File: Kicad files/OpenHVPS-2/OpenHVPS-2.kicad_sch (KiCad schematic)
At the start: 67 parts, among them J1 Conn_01x03_Male, J2 Conn_01x03_Male, Q1 FQT7N10, Q2 BC846, Q3 MMDT3906, U1 74HC14, U2 MAX4162, U3 CD14538BM, U4 MAX6008AEUR+T

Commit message: layout chnages
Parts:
- removed J2: Conn_01x03_Male, Connector_PinHeader_2.54mm:PinHeader_1x03_P2.54mm_Vertical, symbol Connector:Conn_01x03_Male
- added J1: Conn_01x03_Male, Connector_PinHeader_2.54mm:PinHeader_1x03_P2.54mm_Vertical, symbol Connector:Conn_01x03_Male
- added JP1: SolderJumper_2_Open, Jumper:SolderJumper-2_P1.3mm_Open_RoundedPad1.0x1.5mm, symbol Jumper:SolderJumper_2_Open
- added R2: 10M, Resistor_SMD:R_1206_3216Metric, symbol Device:R
- R1: renamed from R7; value 4M7 -> 10M
- renumbered C14 to C1, C19 to C10, C5 to C11, C6 to C12, C7 to C13, C8 to C14, C20 to C15, C9 to C16, C10 to C17, C11 to C18, C21 to C19, C15 to C2, C12 to C20, C13 to C21, C16 to C3, C17 to C4, C18 to C5, C1 to C6, C2 to C7, C3 to C8, C4 to C9, D8 to D1, D9 to D2, D1 to D3, D2 to D4, D3 to D5, D4 to D6, D5 to D7, D6 to D8, D7 to D9, FB2 to FB1, FB1 to FB2, H2 to H1, H5 to H2, J1 to J2, R1 to R10, R12 to R11, R13 to R12, R14 to R13, R15 to R14, R16 to R15, R17 to R16, R18 to R17, R19 to R18, R20 to R19, R6 to R20, R5 to R23, R8 to R3, R9 to R4, R10 to R5, R11 to R6, R4 to R7, R3 to R8, R2 to R9, U4 to U1, U1 to U2, U2 to U3, U3 to U4
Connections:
- net +3V3: now also J1.1 (Pin_1)
- net GND: now also J1.2 (Pin_2)
- net at C21.2, D9.3 (K), R1.1: now also R2.1
- net at D2.2 (A), J2.3 (Pin_3), U4.6 (Q): now also J1.3 (Pin_3)
- net at H2.1, R1.2: now also JP1.2 (B)
- new net: JP1.1 (A), R2.2
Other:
- title: OpenRover -> SafePulse
- moved on the sheet: R21

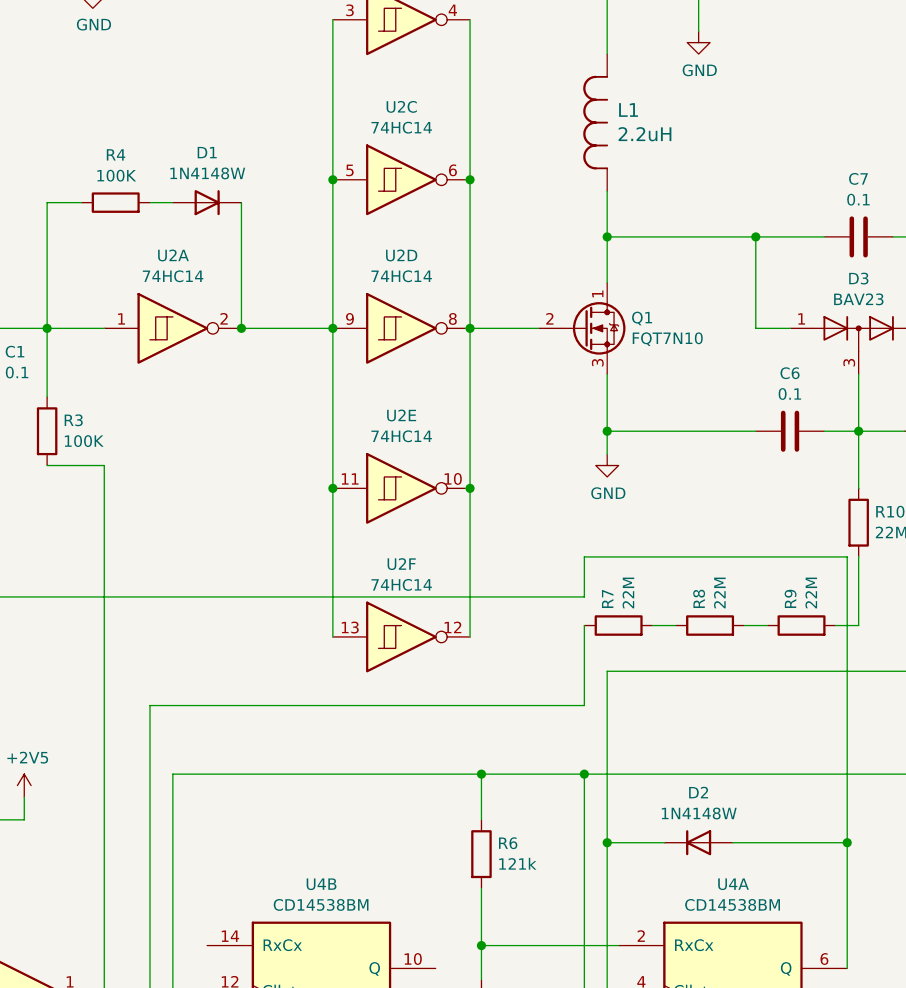
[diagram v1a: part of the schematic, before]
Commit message: Change the diodes
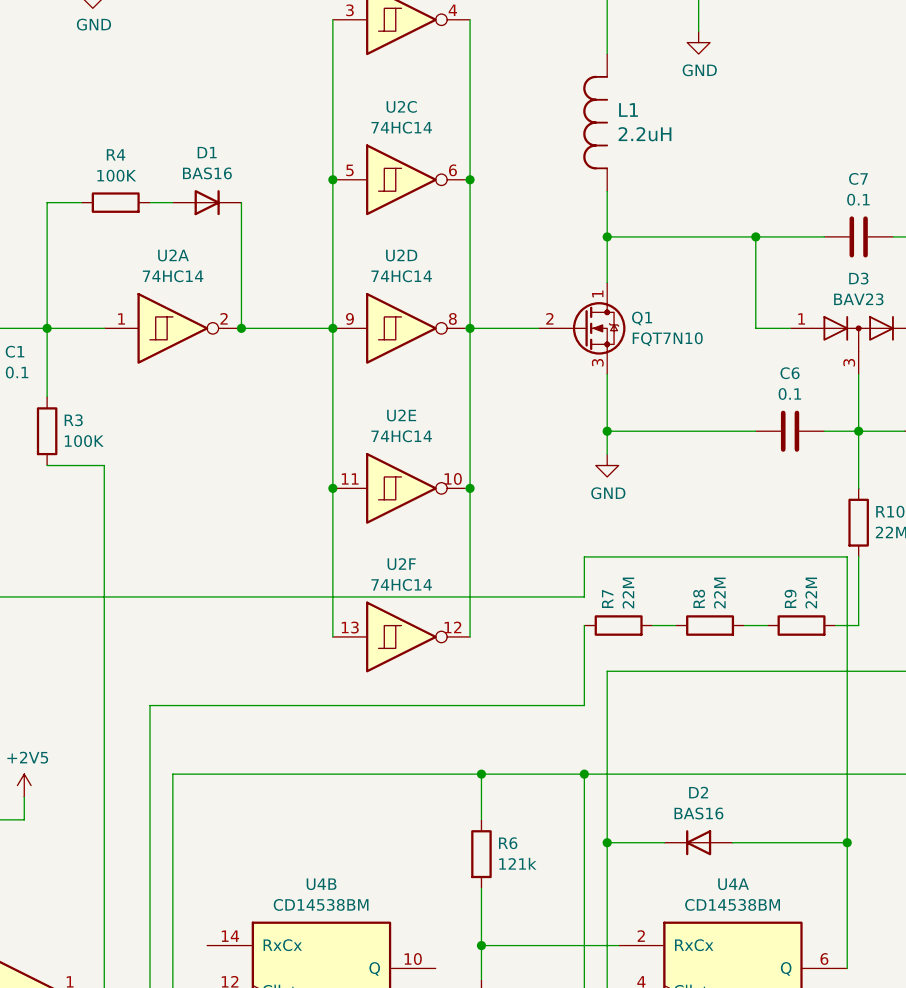
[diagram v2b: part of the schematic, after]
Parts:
- D1, D2: value 1N4148W -> BAS16; footprint Diode_SMD:D_SOD-123 -> Diode_SMD:D_SOT-23_ANK
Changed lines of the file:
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@@
     (in_bom yes) (on_board yes)
     (property "Reference" "D1" (id 0) (at 71.12 68.7832 0))
-    (property "Value" "1N4148W" (id 1) (at 71.12 71.0946 0))
-    (property "Footprint" "Diode_SMD:D_SOD-123" (id 2) (at 71.12 69.85 0)
+    (property "Value" "BAS16" (id 1) (at 71.12 71.095 0))
+    (property "Footprint" "Diode_SMD:D_SOT-23_ANK" (id 2) (at 71.12 69.85 0)
       (effects (font (size 1.27 1.27)) hide)
     )
@@
     (in_bom yes) (on_board yes)
     (property "Reference" "D2" (id 0) (at 125.73 139.9032 0))
-    (property "Value" "1N4148W" (id 1) (at 125.73 142.2146 0))
-    (property "Footprint" "Diode_SMD:D_SOD-123" (id 2) (at 125.73 149.86 0)
+    (property "Value" "BAS16" (id 1) (at 125.73 142.2146 0))
+    (property "Footprint" "Diode_SMD:D_SOT-23_ANK" (id 2) (at 125.73 149.86 0)
       (effects (font (size 1.27 1.27)) hide)
     )
@@
     )
     (path "/00000000-0000-0000-0000-0000600ddc6a"
-      (reference "D1") (unit 1) (value "1N4148W") (footprint "Diode_SMD:D_SOD-123")
+      (reference "D1") (unit 1) (value "BAS16") (footprint "Diode_SMD:D_SOT-23_ANK")
     )
     (path "/00000000-0000-0000-0000-00006007dc1b"
-      (reference "D2") (unit 1) (value "1N4148W") (footprint "Diode_SMD:D_SOD-123")
+      (reference "D2") (unit 1) (value "BAS16") (footprint "Diode_SMD:D_SOT-23_ANK")
     )
     (path "/00000000-0000-0000-0000-00005ff5fed2"

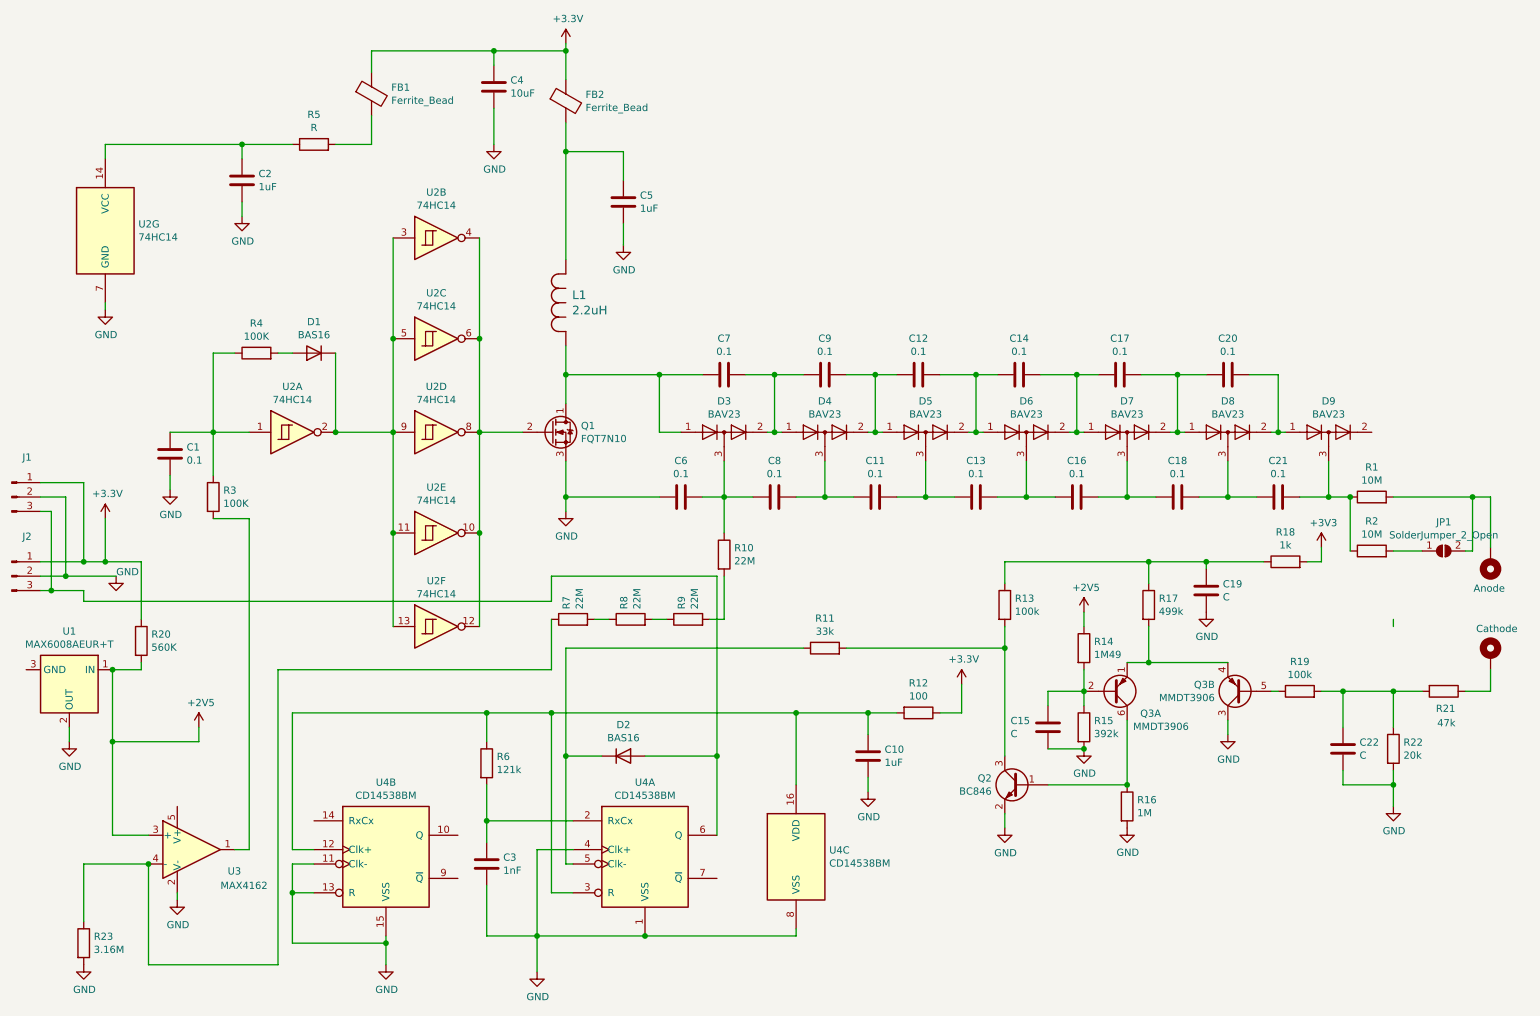
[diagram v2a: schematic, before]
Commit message: Sanity checks, parts shuffling, optimize copper pours
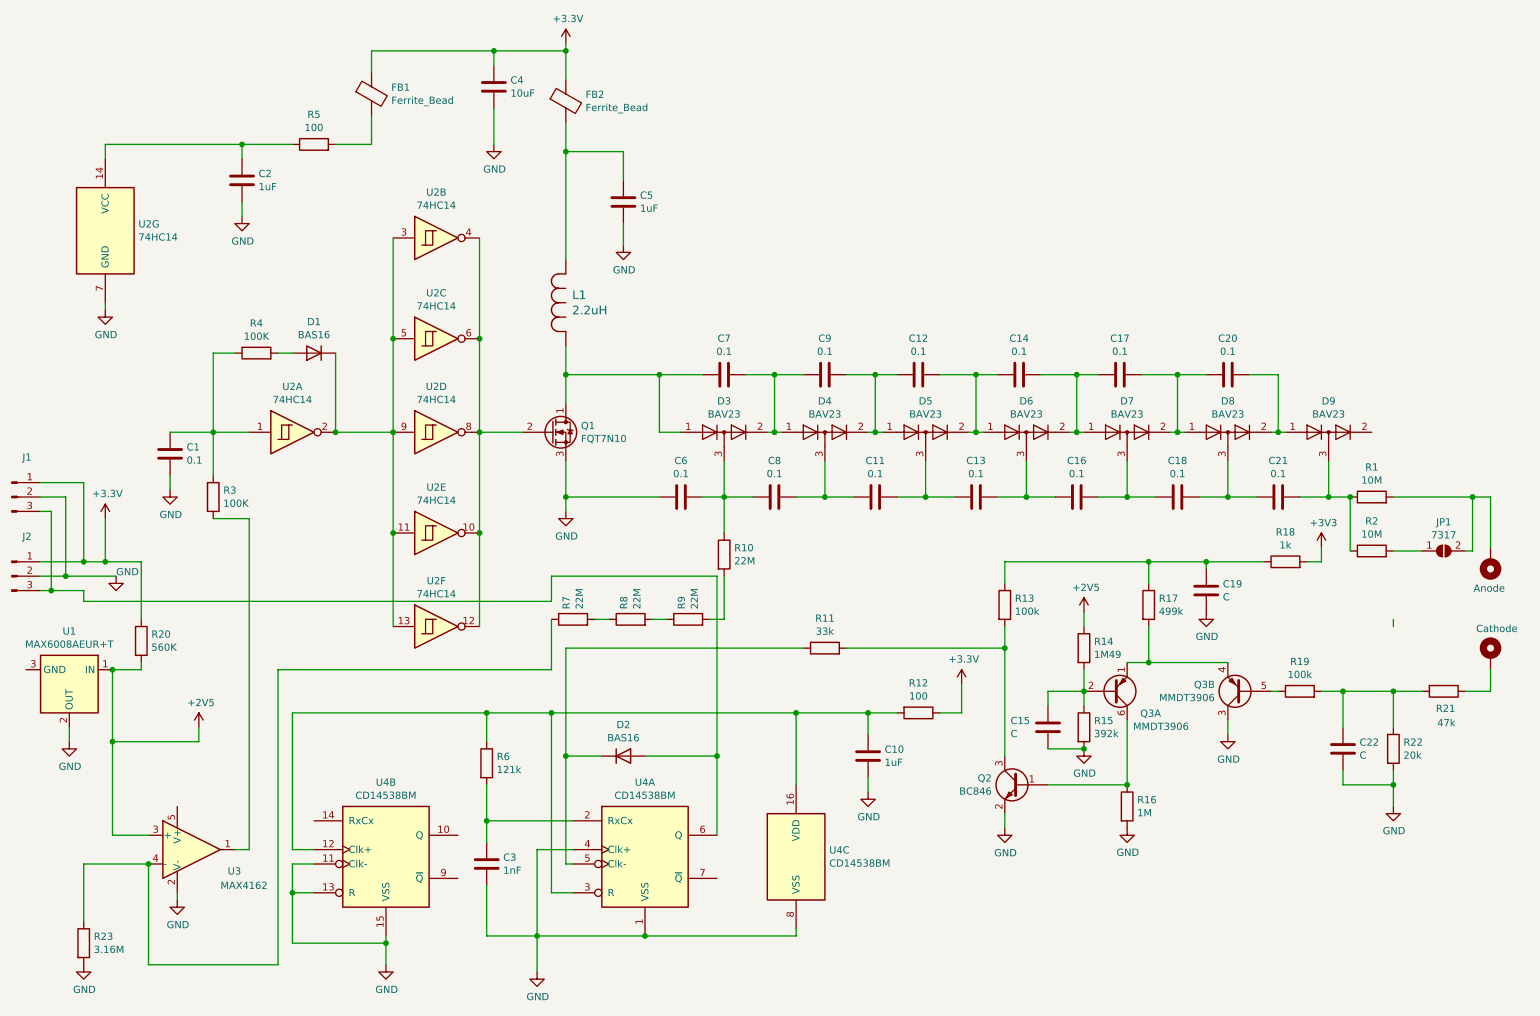
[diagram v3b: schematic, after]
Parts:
- JP1: value SolderJumper_2_Open -> 7317
- R5: value R -> 100
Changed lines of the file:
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@@
     (in_bom yes) (on_board yes)
     (property "Reference" "R5" (id 0) (at 71.12 32.2072 90))
-    (property "Value" "R" (id 1) (at 71.12 34.5186 90))
+    (property "Value" "100" (id 1) (at 71.12 34.519 90))
     (property "Footprint" "Resistor_SMD:R_0805_2012Metric" (id 2) (at 71.12 39.243 90)
       (effects (font (size 1.27 1.27)) hide)
@@
     (in_bom yes) (on_board yes)
     (property "Reference" "JP1" (id 0) (at 270.51 104.1208 0))
-    (property "Value" "SolderJumper_2_Open" (id 1) (at 270.51 106.4195 0))
+    (property "Value" "7317" (id 1) (at 270.51 106.42 0))
     (property "Footprint" "Jumper:SolderJumper-2_P1.3mm_Open_RoundedPad1.0x1.5mm" (id 2) (at 270.51 109.22 0)
       (effects (font (size 1.27 1.27)) hide)
@@
     )
     (path "/d360b2ba-8c27-440f-a077-ab04596b2cba"
-      (reference "JP1") (unit 1) (value "SolderJumper_2_Open") (footprint "Jumper:SolderJumper-2_P1.3mm_Open_RoundedPad1.0x1.5mm")
+      (reference "JP1") (unit 1) (value "7317") (footprint "Jumper:SolderJumper-2_P1.3mm_Open_RoundedPad1.0x1.5mm")
     )
     (path "/00000000-0000-0000-0000-00005ffe44be"
@@
     )
     (path "/00000000-0000-0000-0000-00006009bd6d"
-      (reference "R5") (unit 1) (value "R") (footprint "Resistor_SMD:R_0805_2012Metric")
+      (reference "R5") (unit 1) (value "100") (footprint "Resistor_SMD:R_0805_2012Metric")
     )
     (path "/00000000-0000-0000-0000-000060011a2b"

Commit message: BOM mostly done. cleaned up component labels
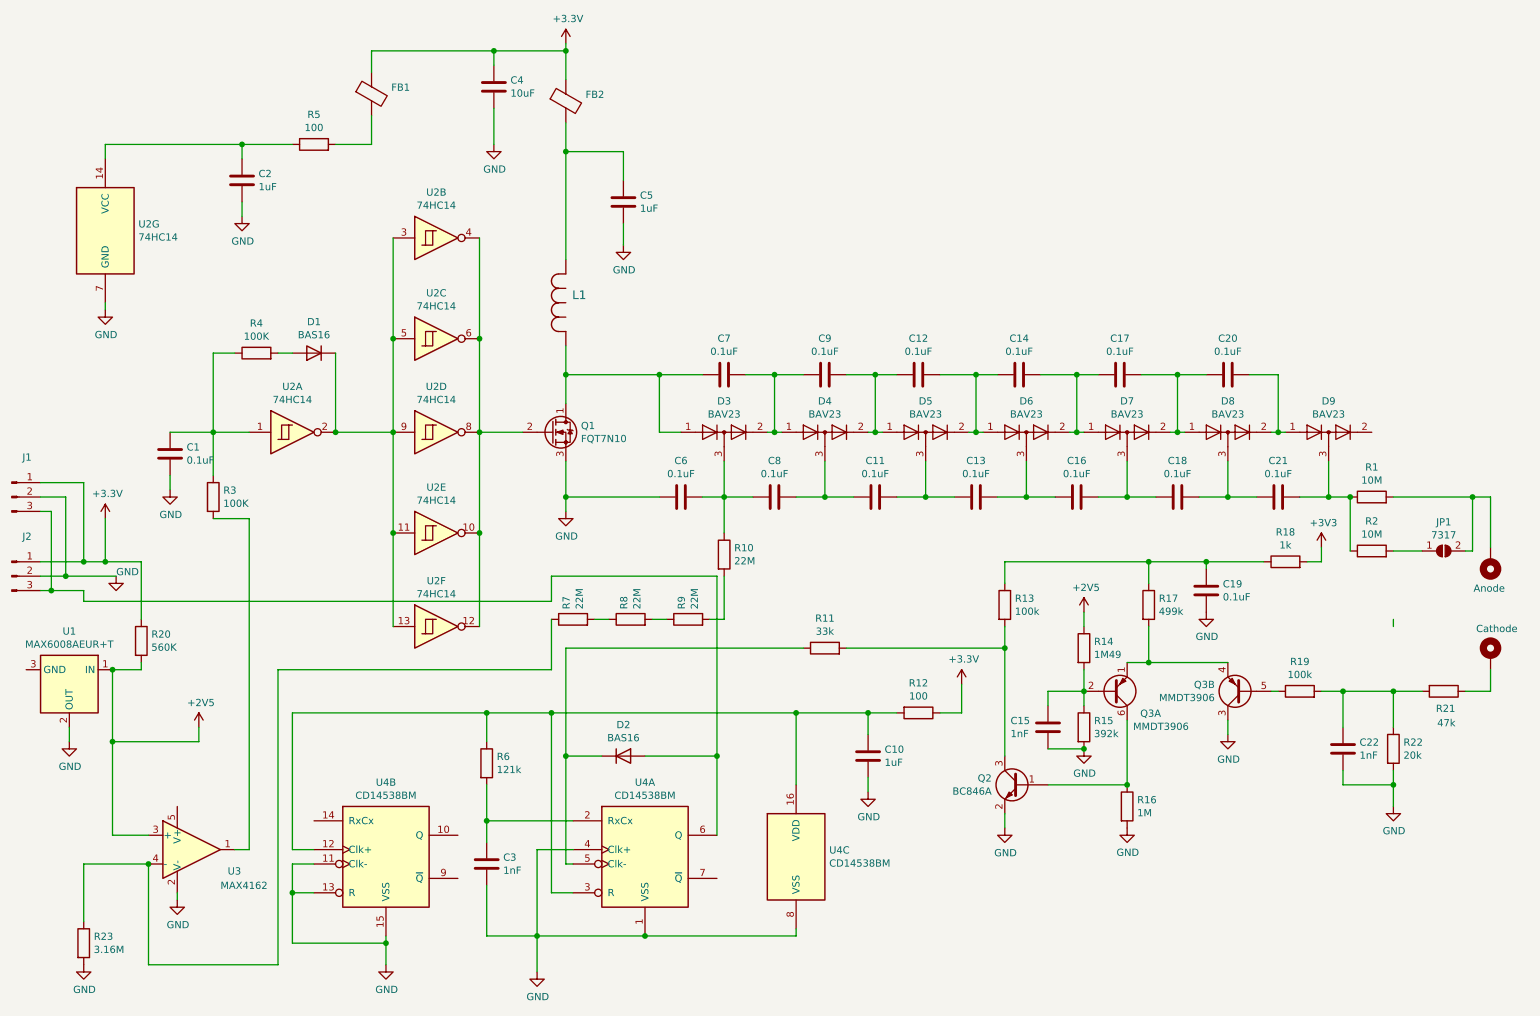
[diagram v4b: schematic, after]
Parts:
- C1: value 0.1 -> 0.1uF
- C11, C12, C13, C14, C16, C17, C18, C20, C21, C6, C7, C8, C9: value 0.1 -> 0.1uF; footprint Resistor_SMD:R_0805_2012Metric -> Capacitor_SMD:C_0805_2012Metric
- C15, C22: value C -> 1nF
- C19: value C -> 0.1uF
- FB1, FB2: value Ferrite_Bead -> BKP2125HS221-T
- L1: value 2.2uH -> NRS6020T2R2NMGJ
- Q2: value BC846 -> BC846A
